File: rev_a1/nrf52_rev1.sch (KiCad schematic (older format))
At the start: 32 parts, among them P1 CONN_01X18, P2 CONN_01X18, P3 USB_OTG, P4 ANTENNA_2_4GHZ, U1 nRF52832, U2 CP2102, U3 LT1129CST-3.3, Y1 32K, Y2 32M

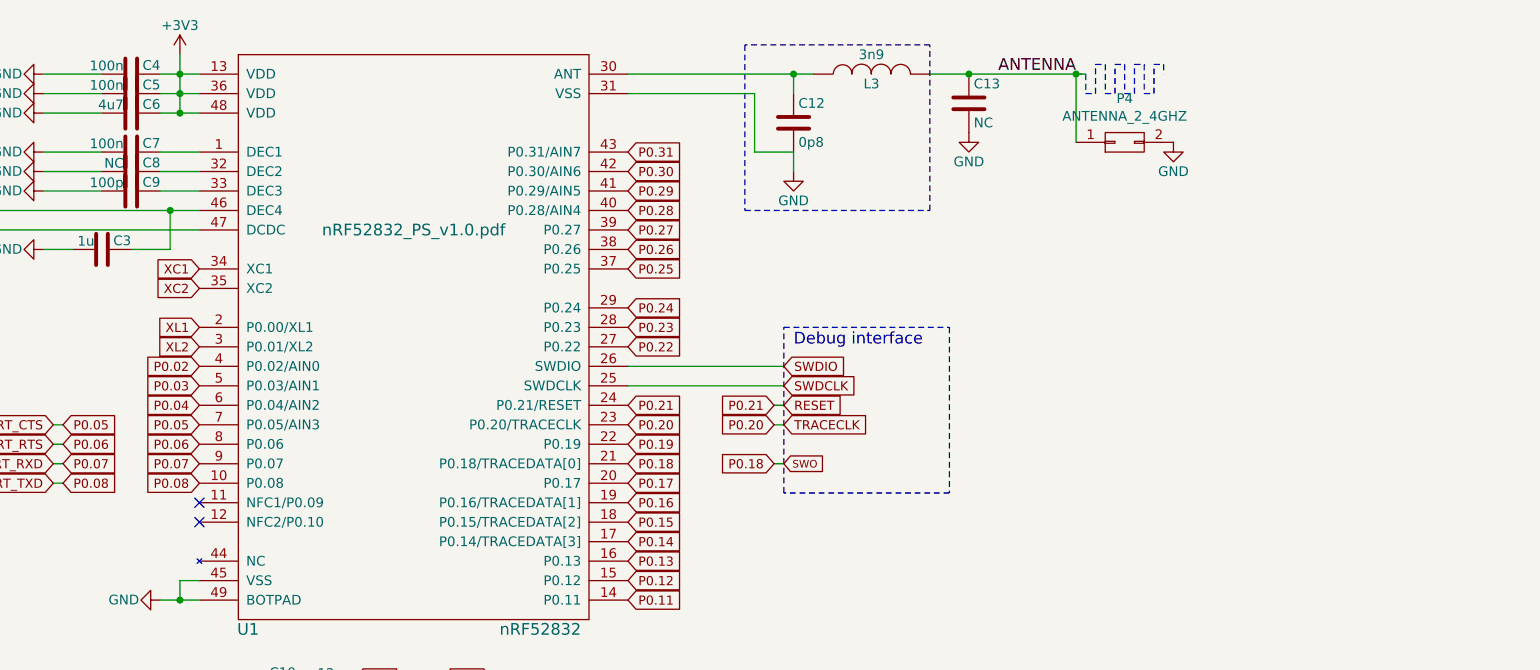
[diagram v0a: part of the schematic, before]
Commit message: Fixed antenna caps
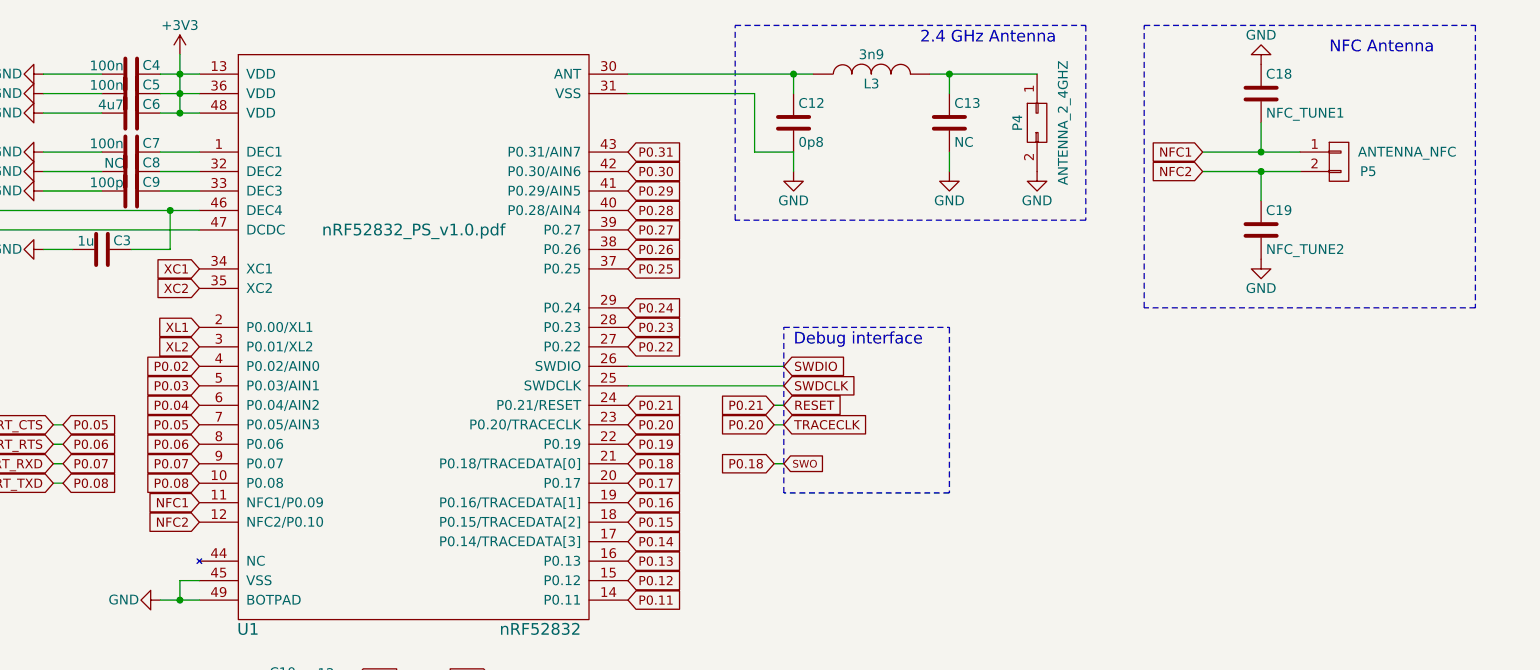
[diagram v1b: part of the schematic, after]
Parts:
- added C18: NFC_TUNE1, RuuviTag:0603_CAP, symbol C
- added C19: NFC_TUNE2, RuuviTag:0603_CAP, symbol C
- added P5: ANTENNA_NFC, symbol CONN_01X02
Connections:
- net GND: now also C18.1, C19.2
- net NFC1: now reaches U1.11 (NFC1/P0.09)
- net NFC1: now also C18.2, P5.1 (P1)
- net NFC2: now reaches U1.12 (NFC2/P0.10)
- net NFC2: now also C19.1, P5.2 (P2)
- net ANTENNA: no longer names the net of C13.1, L3.2, P4.1 (P1)
- no-connect marks 20 -> 18
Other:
- note added: "2.4 GHz Antenna"
- note added: "NFC Antenna"
- moved on the sheet: C13, P4

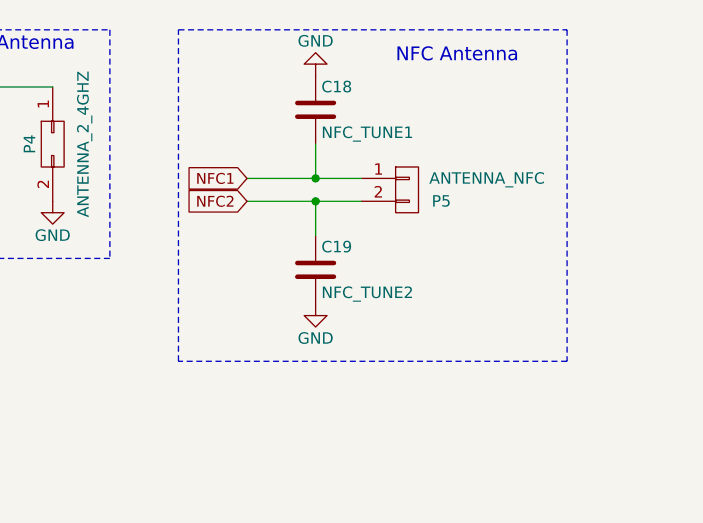
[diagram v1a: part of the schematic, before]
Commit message: Fixed antenna caps
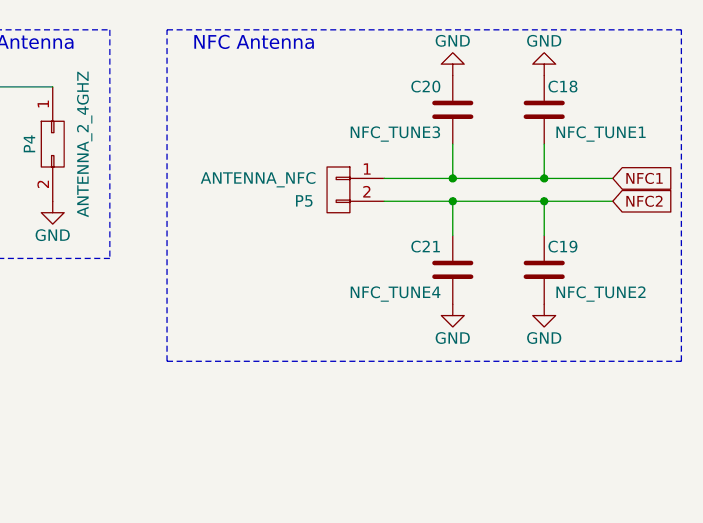
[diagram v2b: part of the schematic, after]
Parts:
- added C20: NFC_TUNE3, RuuviTag:0603_CAP, symbol C
- added C21: NFC_TUNE4, RuuviTag:0603_CAP, symbol C
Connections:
- net GND: now also C20.1, C21.2
- net NFC1: now also C20.2
- net NFC2: now also C21.1
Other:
- moved on the sheet: C18, C19, P5

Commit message: uhh, hope this works
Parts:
- removed C16: 4u7, RuuviTag:0603_CAP, symbol C
- removed C17: 100n, RuuviTag:0603_CAP, symbol C
- removed P3: USB_OTG, Connect:USB_Micro-B, symbol USB_OTG
- removed R1: 4k7, RuuviTag:0603_RES, symbol R
- removed U2: CP2102, Housings_DFN_QFN:QFN-28-1EP_5x5mm_Pitch0.5mm, symbol CP2102
- added JP1, JP2: Jumper_NO_Small, xil_assets:SolderBridgeLarge, symbol Jumper_NO_Small
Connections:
- net P0.05: now also JP2.2
- net P0.06: now also JP1.2
- new net CP2102/UART_CTS: JP2.1
- new net CP2102/UART_RTS: JP1.1
- no-connect marks 18 -> 0
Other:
- note removed: "Configured to bypass internal regulator.\nUses our 5v to 3v3 regulator."
- moved on the sheet: C14, C15, D1, D2, U3
